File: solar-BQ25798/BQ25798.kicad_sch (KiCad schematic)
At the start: 45 parts, among them J1701 Conn_01x02, Q1701 CSD17581Q3A, Q1702 CSD17581Q3A, U1701 BQ25798RQMR, U1702 HT75xx-1-SOT89

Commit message: BQ25798 WIP
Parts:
- Q1701, Q1702: value CSD17581Q3A -> CSD17578Q3A; symbol Transistor_FET:CSD17581Q3A -> cacophony-library:CSD17578Q3A; LCSC Part C2866708 -> C205986
- renumbered C1708 to C1701, C1722 to C1702, C1721 to C1703, C1705 to C1704, C1706 to C1705, C1707 to C1706, C1715 to C1707, C1718 to C1708, C1719 to C1710, C1723 to C1711, C1710 to C1712, C1711 to C1713, C1712 to C1714, C1713 to C1715, C1701 to C1716, C1714 to C1717, C1720 to C1718, C1702 to C1719, C1703 to C1720, C1716 to C1721, C1704 to C1722, C1717 to C1723, D1702 to D1701, D1703 to D1702, D1701 to D1703, R1704 to R1701, R1710 to R1702, R1711 to R1703, R1706 to R1704, R1701 to R1705, R1707 to R1706, R1702 to R1707, R1703 to R1708, R1705 to R1710, U1702 to U1701, U1701 to U1702

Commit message: Solar battery WIP
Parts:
- removed C1702, C1703: 1uF, Capacitor_SMD:C_0603_1608Metric, symbol Device:C_Small
- removed D1701, D1702: D, Diode_SMD:D_SOD-323_HandSoldering, symbol Device:D
- removed D1703: D_Shockley, Diode_SMD:D_SOD-523, symbol Device:D_Shockley
- removed J1701: Conn_01x02, Connector_PinHeader_2.54mm:PinHeader_1x02_P2.54mm_Vertical, symbol Connector_Generic:Conn_01x02
- removed Q1701, Q1702: CSD17578Q3A, Package_SON:VSON-8_3.3x3.3mm_P0.65mm_NexFET, symbol cacophony-library:CSD17578Q3A
- removed R1702, R1703: 10k, Resistor_SMD:R_0402_1005Metric, symbol Device:R
- removed U1701: HT75xx-1-SOT89, Package_TO_SOT_SMD:SOT-89-3, symbol Regulator_Linear:HT75xx-1-SOT89
- added C1708, C1719: 100uF 50V, Capacitor_THT:CP_Radial_D6.3mm_P2.50mm, symbol Device:C_Polarized
- L1701: footprint cacophony-library:IND-SMD_L11.3-W10.0_XAL1010-332ME -> Inductor_SMD:L_TDK_SLF10165; LCSC Part C6358489 -> C2991822
- renumbered C1716 to C1701, C1719 to C1702, C1720 to C1703, C1722 to C1704, C1704 to C1705, C1705 to C1706, C1706 to C1707, C1701 to C1709, C1709 to C1710, C1712 to C1711, C1713 to C1712, C1714 to C1713, C1715 to C1714, C1717 to C1715, C1721 to C1716, C1723 to C1717, C1707 to C1718, C1718 to C1720, C1708 to C1721, C1710 to C1722, C1711 to C1723, D1704 to D1701, R1705 to R1701, R1707 to R1702, R1701 to R1703, R1708 to R1704, R1710 to R1705, R1704 to R1707, R1709 to R1708, U1702 to U1701
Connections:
- net VBUS is gone; now on net V_{IN}: C1705.1, C1706.1, C1707.1, U1701.2 (VBUS), U1701.3 (VBUS), U1701.8 (VAC2)
- net GND: now also U1701.11 (ACDRV1), C1708.2, C1719.2
- net PACK_+: now also C1716.1, C1717.1, R1705.2, U1701.22 (BAT), U1701.23 (BAT), C1719.1
- net V_{IN}: now also C1708.1
- net STAT_PHY: now reaches D1701.1 (K), U1701.1 (STAT)
- net STAT: now reaches D1701.2 (A), R1707.2
- net TS: now reaches R1706.2, R1708.1, TH1701.2, U1701.16 (TS)
- net BATP: now reaches C1720.2, R1705.1, U1701.18 (BATP)
- net D+: no longer names the net of U1701.6 (D+)
- net D-: no longer names the net of U1701.7 (D-)
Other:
- note added: "The host can disable the OOA by setting DIS_FWD_OOA = 1"
- moved on the sheet: C1701, C1702, C1703, C1704, C1705, C1706, C1707, C1709, C1712, C1713, C1714, C1715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

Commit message: Version v0.0.2
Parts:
- C1708, C1719: now not fitted; now left out of the parts list
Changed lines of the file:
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@@
 		(unit 1)
 		(exclude_from_sim no)
-		(in_bom yes)
-		(on_board yes)
-		(dnp no)
+		(in_bom no)
+		(on_board yes)
+		(dnp yes)
 		(fields_autoplaced yes)
 		(property "Reference" "C1719"
@@
 		(unit 1)
 		(exclude_from_sim no)
-		(in_bom yes)
-		(on_board yes)
-		(dnp no)
+		(in_bom no)
+		(on_board yes)
+		(dnp yes)
 		(fields_autoplaced yes)
 		(property "Reference" "C1708"

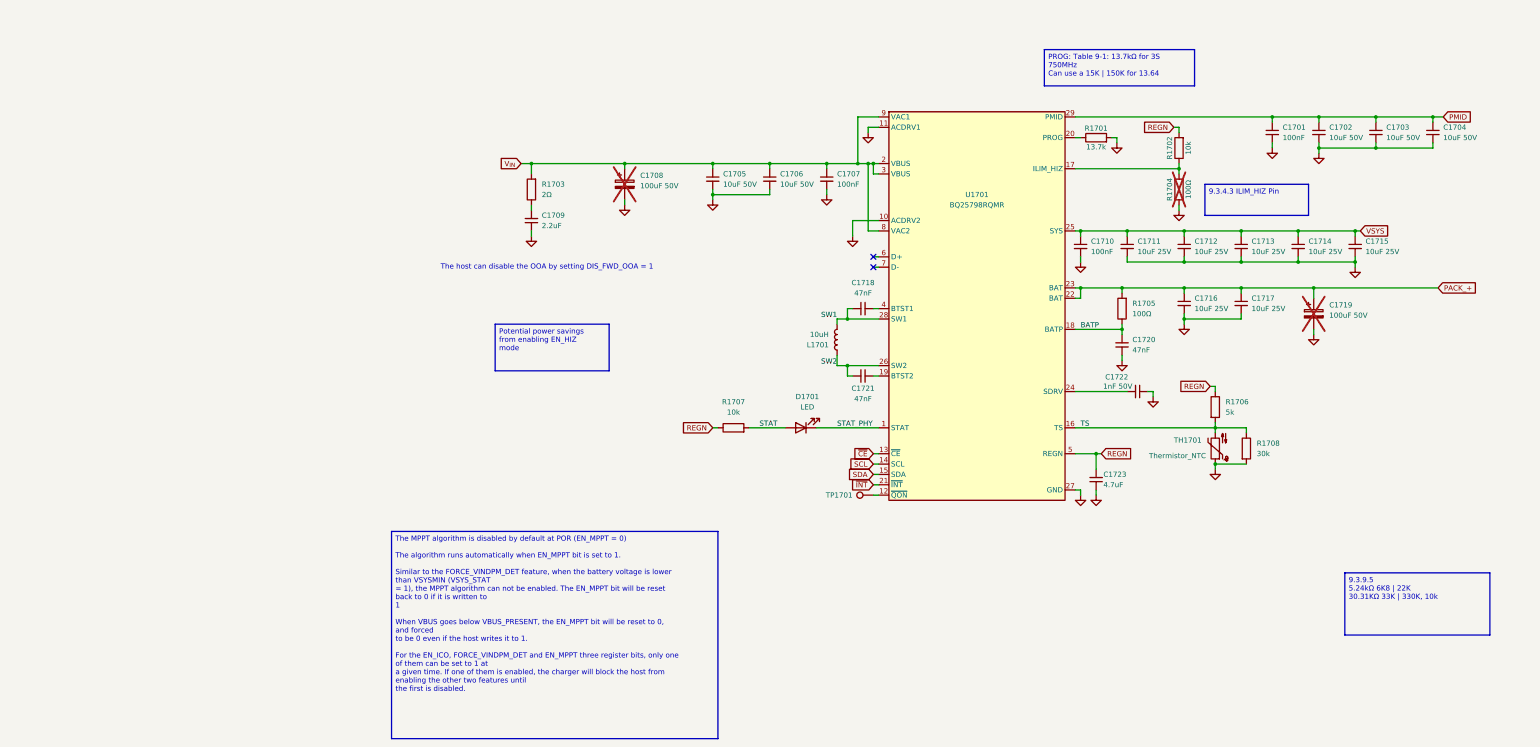
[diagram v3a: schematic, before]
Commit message: Update battery PCB
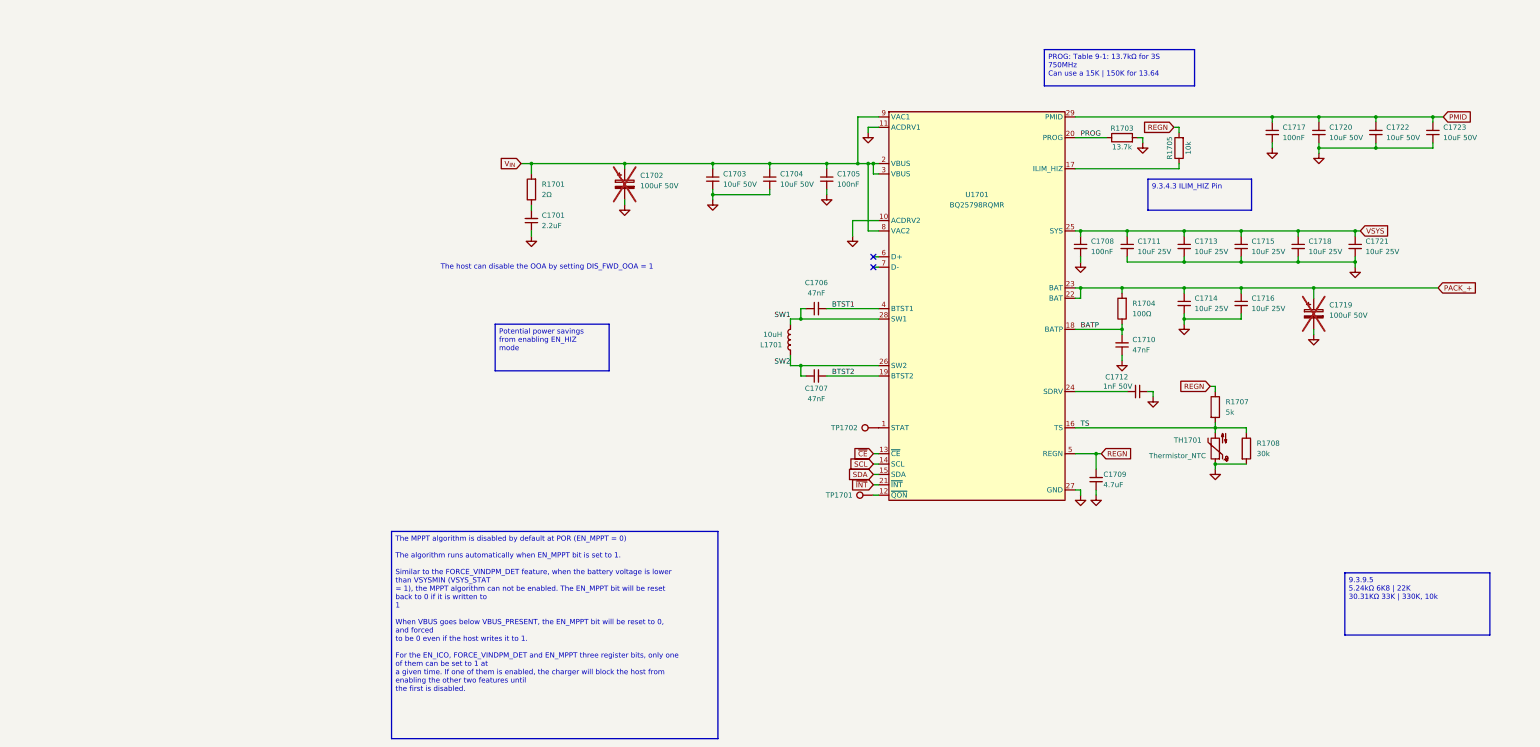
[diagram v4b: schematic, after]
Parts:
- removed D1701: LED, LED_SMD:LED_0603_1608Metric, symbol Device:LED
- removed R1704: 100Ω, Resistor_SMD:R_0402_1005Metric, symbol Device:R
- removed R1707: 10k, Resistor_SMD:R_0402_1005Metric, symbol Device:R
- added TP1702: TestPoint, cacophony-library:TP_PAD, symbol cacophony-library:TestPoint
- C1706: renamed from C1718; footprint Capacitor_SMD:C_0603_1608Metric -> Capacitor_SMD:C_0402_1005Metric; LCSC Part C1622 -> C307339
- C1707: renamed from C1721; footprint Capacitor_SMD:C_0603_1608Metric -> Capacitor_SMD:C_0402_1005Metric; LCSC Part C1622 -> C307339
- C1710: renamed from C1720; footprint Capacitor_SMD:C_0603_1608Metric -> Capacitor_SMD:C_0402_1005Metric; LCSC Part C1622 -> C307339
- L1701: footprint Inductor_SMD:L_TDK_SLF10165 -> Inductor_SMD:L_12x12mm_H8mm; LCSC Part C2991822 -> C167261
- renumbered C1709 to C1701, C1708 to C1702, C1705 to C1703, C1706 to C1704, C1707 to C1705, C1710 to C1708, C1723 to C1709, C1722 to C1712, C1712 to C1713, C1716 to C1714, C1713 to C1715, C1717 to C1716, C1701 to C1717, C1714 to C1718, C1702 to C1720, C1715 to C1721, C1703 to C1722, C1704 to C1723, R1703 to R1701, R1701 to R1703, R1705 to R1704, R1702 to R1705, R1706 to R1707
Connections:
- net BTST1: now reaches C1706.2, U1701.4 (BTST1)
- net PROG: now reaches R1703.1, U1701.20 (PROG)
- net BTST2: now reaches C1707.2, U1701.19 (BTST2)
- net STAT_PHY: no longer names the net of U1701.1 (STAT)
- net STAT_PHY: now also TP1702.1
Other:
- moved on the sheet: C1706, C1707, L1701, R1703
